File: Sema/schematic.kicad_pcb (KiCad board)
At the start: 2 copper layers, 98.8 x 91 mm, 80 parts, among them J1 Conn_01x05_Male, J10 Conn_01x05_Male, J11 Conn_01x05_Male, J12 Conn_01x05_Male, J3 Conn_01x03_Male, J4 Conn_01x05_Male, J5 Conn_01x03_Male, J7 Conn_01x05_Male, J8 Conn_01x05_Male, J9 Conn_01x05_Male, U1 LM317AT/NOPB, U10 74LVT573MTC, U11 74LVT573MTC, U12 74LVT573MTC, U13 74LVT573MTC, U14 ULN2003AIDR, U15 ULN2003AIDR, U16 ULN2003AIDR, U17 ULN2003AIDR, U2 LM317AT/NOPB, U3 PIC24FJ64GA702-I/SO, U4 ABLS-8.000MHZ-B2-T, U5 FT232RL, U6 CD74HC4514M96, U7 PTMUX1308QDYYRQ1, U8 74LVT573MTC, U9 74LVT573MTC

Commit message: Male izmjene oko labela
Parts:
- 0.1uF1: value 08055A220JAT2A -> 0.1uF

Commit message: Izmjene na layout-u
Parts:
- removed POWER 12V: Conn_01x02_Male, Connector_PinHeader_1.00mm:PinHeader_1x02_P1.00mm_Vertical
- added J13: Conn_01x01_Male, Connector_PinHeader_1.00mm:PinHeader_1x01_P1.00mm_Vertical, F.Cu at (78.6, 39.6)
- added J14: Conn_01x01_Male, Connector_PinHeader_1.00mm:PinHeader_1x01_P1.00mm_Vertical, F.Cu at (54.0, 74.0)
- added J15: Conn_01x01_Male, Connector_PinHeader_1.00mm:PinHeader_1x01_P1.00mm_Vertical, F.Cu at (54.0, 78.0)
- added J16: Conn_01x01_Male, Connector_PinHeader_1.00mm:PinHeader_1x01_P1.00mm_Vertical, F.Cu at (125.0, 112.2)
- added J2: Conn_01x01_Male, Connector_PinHeader_1.00mm:PinHeader_1x01_P1.00mm_Vertical, F.Cu at (74.0, 39.6)
- added TP1: TestPoint, Connector_PinHeader_1.00mm:PinHeader_1x01_P1.00mm_Vertical, F.Cu at (50.0, 50.4)
- added TP10: TestPoint, Connector_PinHeader_1.00mm:PinHeader_1x01_P1.00mm_Vertical, F.Cu at (120.6, 118.6)
- added TP11: TestPoint, Connector_PinHeader_1.00mm:PinHeader_1x01_P1.00mm_Vertical, F.Cu at (123.6, 118.6)
- added TP2: TestPoint, Connector_PinHeader_1.00mm:PinHeader_1x01_P1.00mm_Vertical, F.Cu at (71.6, 53.2)
- added TP3: TestPoint, Connector_PinHeader_1.00mm:PinHeader_1x01_P1.00mm_Vertical, F.Cu at (78.0, 47.4)
- added TP4: TestPoint, Connector_PinHeader_1.00mm:PinHeader_1x01_P1.00mm_Vertical, F.Cu at (70.0, 70.2)
- added TP5: TestPoint, Connector_PinHeader_1.00mm:PinHeader_1x01_P1.00mm_Vertical, F.Cu at (67.2, 70.2)
- added TP6: TestPoint, Connector_PinHeader_1.00mm:PinHeader_1x01_P1.00mm_Vertical, F.Cu at (107.8, 118.6)
- added TP7: TestPoint, Connector_PinHeader_1.00mm:PinHeader_1x01_P1.00mm_Vertical, F.Cu at (111.2, 118.6)
- added TP8: TestPoint, Connector_PinHeader_1.00mm:PinHeader_1x01_P1.00mm_Vertical, F.Cu at (114.4, 118.6)
- added TP9: TestPoint, Connector_PinHeader_1.00mm:PinHeader_1x01_P1.00mm_Vertical, F.Cu at (117.4, 118.6)
- 0.1uF1: value 0.1uF -> 08055A220JAT2A
- moved J11 13.0 mm to (135.3, 119.0), turned to -90 degrees
- moved J10 11.6 mm to (142.8, 110.0)
- moved J12 7.47 mm to (142.8, 94.4)
- moved J9 6.69 mm to (142.8, 80.4)
- moved H4 3.35 mm to (53.6, 124.4)
- moved J4 3.29 mm to (91.7, 55.2)
- moved J8 3.20 mm to (142.8, 66.6)
- moved H3 2.41 mm to (141.6, 124.6)
- moved J3 2.21 mm to (68.6, 56.4)
- moved J5 1.81 mm to (76.2, 60.6)
- moved C14 1.71 mm to (120.0, 42.2), turned to 180 degrees
- moved C20 1.71 mm to (133.2, 80.8)
- moved J7 1.49 mm to (142.7, 53.2)
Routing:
- net E1: track 55.3 -> 104.6 mm, vias 2 -> 3
- net E3: track 25.9 -> 74.8 mm, vias 2 -> 3
- net E4: track 18.6 -> 66.2 mm, vias 2 -> 3
- net E5: track 25.7 -> 73.3 mm, vias 2 -> 3
- net E2: track 43.3 -> 90.5 mm, vias 2 -> 3
- net 12V: track 267.7 -> 299.1 mm
- net PGD: track 19.7 -> 39.9 mm
- net B3: track 11.7 -> 24.7 mm
- net B5: track 19.6 -> 32.5 mm
- net GND: track 109.5 -> 121.5 mm, vias 38 -> 42
- net Net-(J3-Pad2): track 21.2 -> 33.0 mm, vias 2 -> 4
- net tx: track 28.6 -> 40.3 mm, vias 0 -> 2
- net PI3: track 11.7 -> 23.2 mm
- net Y6: track 14.5 -> 25.1 mm, vias 0 -> 2
- net PI6: track 14.6 -> 25.0 mm, vias 0 -> 2
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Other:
- board size 98.8 x 91 mm -> 100 x 93 mm

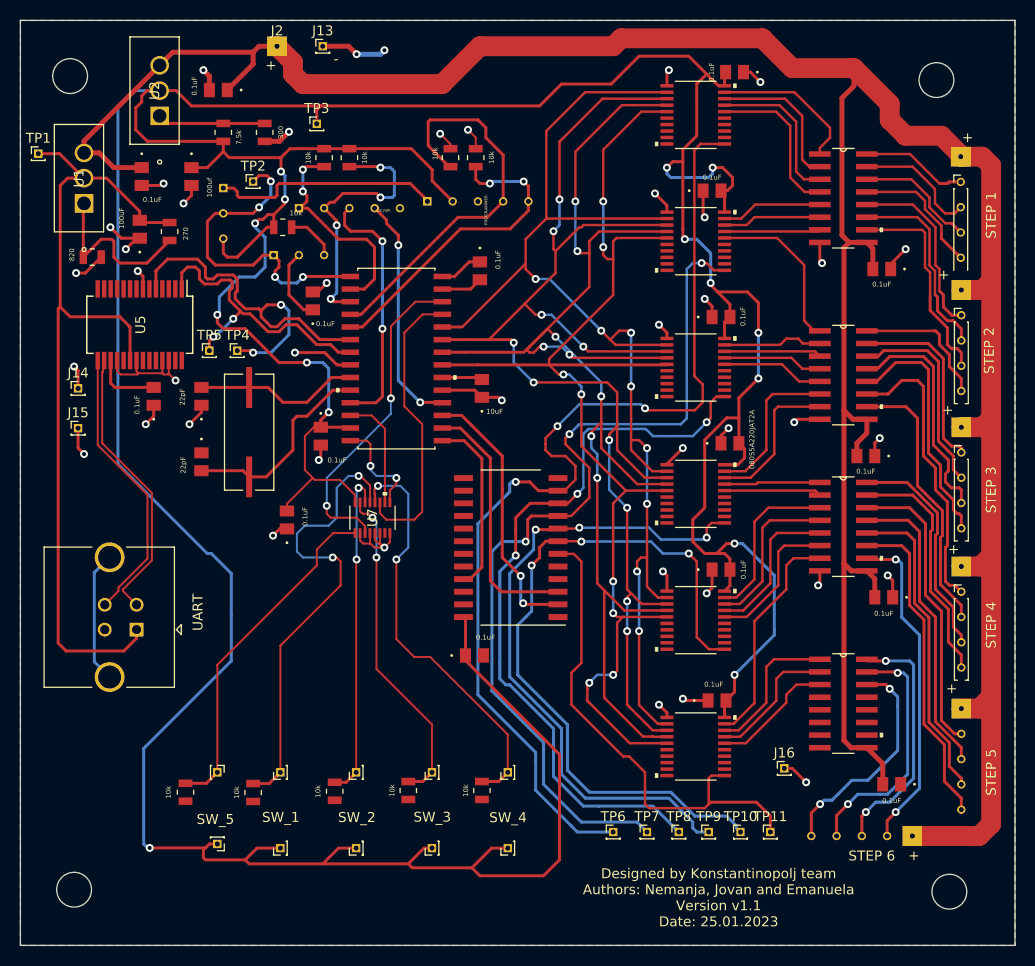
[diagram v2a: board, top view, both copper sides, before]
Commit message: Dodavanje labela
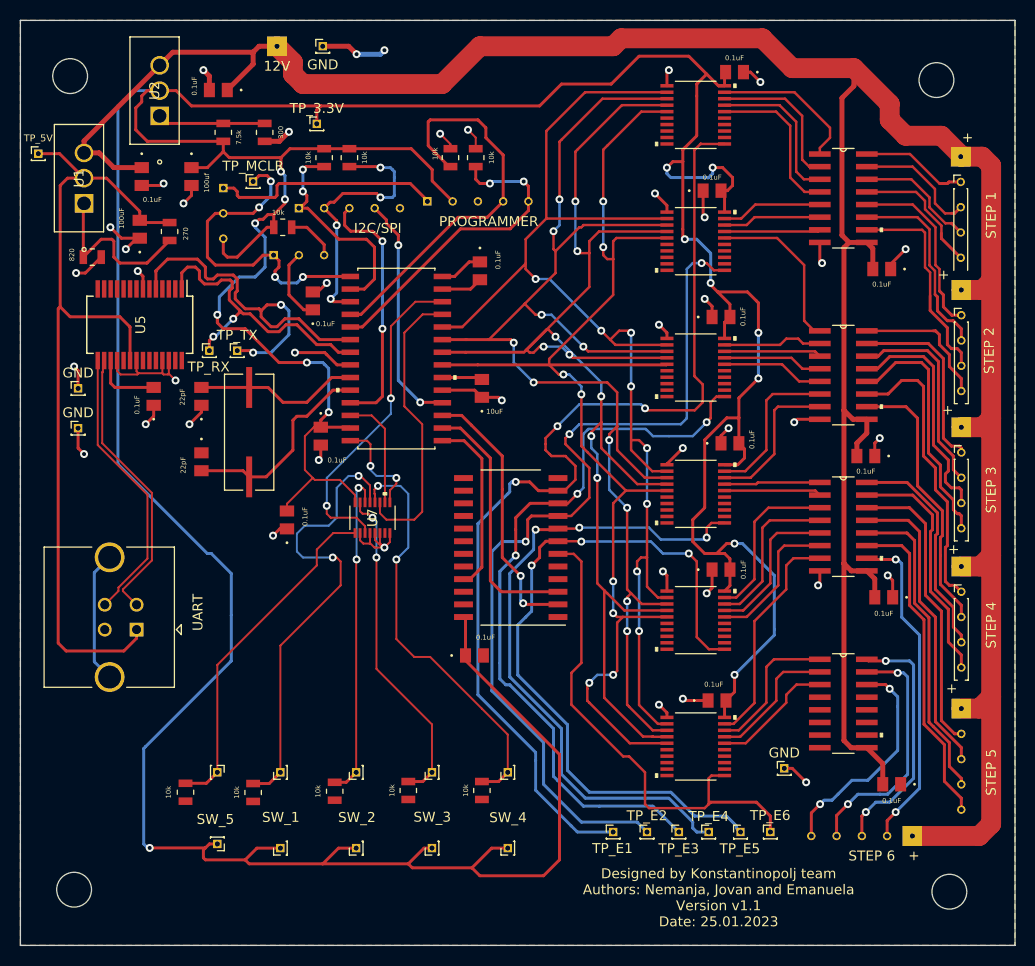
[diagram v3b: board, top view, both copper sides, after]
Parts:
- 0.1uF1: value 08055A220JAT2A -> 0.1uF
- renumbered J2 to 12V, J15 to GND, J14 to GND, J13 to GND, J16 to GND, TP3 to TP_3.3V, TP1 to TP_5V, TP6 to TP_E1, TP7 to TP_E2, TP8 to TP_E3, TP9 to TP_E4, TP10 to TP_E5, TP11 to TP_E6, TP2 to TP_MCLR, TP5 to TP_RX, TP4 to TP_TX
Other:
- board text removed: "-"
